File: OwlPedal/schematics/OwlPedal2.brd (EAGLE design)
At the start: 103.1 x 79.5 mm, 86 parts, among them IC1 TS924, J1 NEUTRIK_NMJ6HCD2, J2 NEUTRIK_NMJ6HCD2, J3 NEUTRIK_NMJ6HCD2, J4 NEUTRIK_NMJ6HCD2, J5 NEUTRIK_NMJ6HCD2, J6 NEUTRIK_NMJ6HCD2, J7 POWER_JACK, SW2 5GTH9, U1 TS5A22364

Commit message: adjusted labels
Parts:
- moved R12 0.38 mm to (63.6, 39.4)
- moved R13 0.38 mm to (67.4, 39.4)
- flipped JP2 to the bottom, turned to 180 degrees
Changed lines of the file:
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@@
 </element>
 <element name="R19" library="Rebel" package="0603" value="1k" x="62.5475" y="36.195" smashed="yes" rot="R90">
-<attribute name="NAME" x="62.1095" y="34.584" size="0.762" layer="25" font="vector" rot="R270"/>
+<attribute name="NAME" x="62.2365" y="34.838" size="0.762" layer="25" font="vector" rot="R270"/>
 </element>
 <element name="R5" library="Rebel" package="0603" value="1M" x="69.85" y="58.674" smashed="yes">
@@
 <attribute name="NAME" x="60.66105625" y="37.57635625" size="0.762" layer="25" font="vector" rot="R180" align="bottom-center"/>
 </element>
-<element name="R12" library="Rebel" package="0603" value="1k" x="63.9445" y="39.37" smashed="yes">
-<attribute name="NAME" x="63.913675" y="40.18240625" size="0.762" layer="25" font="vector" align="bottom-center"/>
+<element name="R12" library="Rebel" package="0603" value="1k" x="63.5635" y="39.37" smashed="yes">
+<attribute name="NAME" x="63.532675" y="40.18240625" size="0.762" layer="25" font="vector" align="bottom-center"/>
 </element>
 <element name="R4" library="Rebel" package="0603" value="560R" x="67.3735" y="53.6575" smashed="yes" rot="R270">
@@
 </element>
 <element name="C19" library="resistor" package="C0603" value="4n7 C0G" x="64.516" y="36.195" smashed="yes" rot="R90">
-<attribute name="NAME" x="64.954" y="33.0435" size="0.762" layer="25" font="vector" rot="R90"/>
+<attribute name="NAME" x="64.954" y="32.7895" size="0.762" layer="25" font="vector" rot="R90"/>
 <attribute name="VALUE" x="66.548" y="35.306" size="1.27" layer="27" rot="R90"/>
 </element>
 <element name="C17" library="resistor" package="C0603" value="2n2 C0G" x="58.6105" y="35.433" smashed="yes" rot="R270">
-<attribute name="NAME" x="57.899" y="33.09" size="0.762" layer="25" font="vector"/>
+<attribute name="NAME" x="57.645" y="33.09" size="0.762" layer="25" font="vector"/>
 <attribute name="VALUE" x="56.5785" y="36.322" size="1.27" layer="27" rot="R270"/>
 </element>
@@
 </element>
 <element name="R22" library="Rebel" package="0603" value="1k" x="68.58" y="36.195" smashed="yes" rot="R90">
-<attribute name="NAME" x="68.12374375" y="33.545515625" size="0.762" layer="25" font="vector" rot="R270" align="bottom-center"/>
+<attribute name="NAME" x="68.25074375" y="33.799515625" size="0.762" layer="25" font="vector" rot="R270" align="bottom-center"/>
 </element>
 <element name="R14" library="Rebel" package="0603" value="2k" x="70.5485" y="39.0525" smashed="yes" rot="R90">
 <attribute name="NAME" x="69.6656625" y="39.110025" size="0.762" layer="25" font="vector" rot="R90" align="bottom-center"/>
 </element>
-<element name="R13" library="Rebel" package="0603" value="1k" x="66.9925" y="39.37" smashed="yes" rot="R180">
-<attribute name="NAME" x="67.008525" y="40.20485625" size="0.762" layer="25" font="vector" align="bottom-center"/>
+<element name="R13" library="Rebel" package="0603" value="1k" x="67.3735" y="39.37" smashed="yes" rot="R180">
+<attribute name="NAME" x="67.389525" y="40.20485625" size="0.762" layer="25" font="vector" align="bottom-center"/>
 </element>
 <element name="C15" library="resistor" package="C0603" value="220p C0G" x="71.5645" y="41.656" smashed="yes">
-<attribute name="NAME" x="71.004640625" y="42.235340625" size="0.762" layer="25" font="vector"/>
+<attribute name="NAME" x="70.750640625" y="42.362340625" size="0.762" layer="25" font="vector"/>
 <attribute name="VALUE" x="70.6755" y="39.624" size="1.27" layer="27"/>
 </element>
 <element name="C20" library="resistor" package="C0603" value="4n7 C0G" x="66.6115" y="36.195" smashed="yes" rot="R90">
-<attribute name="NAME" x="66.1735" y="34.584" size="0.762" layer="25" font="vector" rot="R270"/>
+<attribute name="NAME" x="67.0495" y="32.726" size="0.762" layer="25" font="vector" rot="R90"/>
 <attribute name="VALUE" x="68.6435" y="35.306" size="1.27" layer="27" rot="R90"/>
 </element>
@@
 </element>
 <element name="C13" library="resistor" package="C0603" value="1n C0G" x="66.9925" y="41.783" smashed="yes">
-<attribute name="NAME" x="66.3634375" y="42.489965625" size="0.762" layer="25" font="vector"/>
+<attribute name="NAME" x="66.2364375" y="42.489965625" size="0.762" layer="25" font="vector"/>
 <attribute name="VALUE" x="66.1035" y="39.751" size="1.27" layer="27"/>
 </element>
@@
 <attribute name="NAME" x="79.502" y="21.59" size="1.016" layer="25" font="vector" rot="R270" align="bottom-center"/>
 </element>
-<element name="JP2" library="SparkFun" package="1X04" value="" x="53.0225" y="23.8125" smashed="yes">
-<attribute name="VALUE" x="51.7525" y="20.6375" size="1.27" layer="27"/>
+<element name="JP2" library="SparkFun" package="1X04" value="" x="53.0225" y="23.8125" smashed="yes" rot="MR180">
+<attribute name="VALUE" x="51.7525" y="26.9875" size="1.27" layer="28" rot="MR180"/>
 </element>
 <element name="U2" library="Hangar" package="TSR-1-2450" value="" x="33.02" y="48.26" smashed="yes" rot="R180">
@@
 <via x="94.0435" y="49.4665" extent="1-16" drill="0.3048"/>
 <via x="69.469" y="33.655" extent="1-16" drill="0.3048"/>
-<via x="62.23" y="34.163" extent="1-16" drill="0.3048"/>
+<via x="61.849" y="34.29" extent="1-16" drill="0.3048"/>
 <via x="72.8675" y="50.7775" extent="1-16" drill="0.3048"/>
-<via x="61.976" y="40.3225" extent="1-16" drill="0.3048"/>
-<via x="69.1515" y="40.3225" extent="1-16" drill="0.3048"/>
+<via x="61.976" y="40.5765" extent="1-16" drill="0.3048"/>
+<via x="69.1515" y="40.5765" extent="1-16" drill="0.3048"/>
 <via x="96.9645" y="28.0035" extent="1-16" drill="0.3048"/>
 </signal>
@@
 <contactref element="R18" pad="1"/>
 <via x="62.357" y="32.8295" extent="1-16" drill="0.3048"/>
-<wire x1="60.6425" y1="34.583" x2="60.6425" y2="34.544" width="0.3048" layer="1"/>
-<wire x1="62.357" y1="32.8295" x2="60.6425" y2="34.544" width="0.4064" layer="1"/>
+<wire x1="60.6425" y1="34.583" x2="60.6425" y2="34.29" width="0.4064" layer="1"/>
+<wire x1="62.357" y1="32.8295" x2="62.103" y2="32.8295" width="0.4064" layer="1"/>
+<wire x1="62.103" y1="32.8295" x2="60.6425" y2="34.29" width="0.4064" layer="1"/>
 <contactref element="JP9" pad="1"/>
 <wire x1="75.8825" y1="66.9925" x2="78.74" y2="64.135" width="0.4064" layer="1"/>
@@
 <contactref element="IC1" pad="10"/>
 <contactref element="C12" pad="2"/>
-<wire x1="64.7945" y1="39.37" x2="64.7945" y2="40.083" width="0.4064" layer="1"/>
-<wire x1="64.7945" y1="40.083" x2="63.0945" y2="41.783" width="0.4064" layer="1"/>
+<wire x1="64.4135" y1="39.37" x2="64.4135" y2="40.464" width="0.4064" layer="1"/>
+<wire x1="64.4135" y1="40.464" x2="63.0945" y2="41.783" width="0.4064" layer="1"/>
 <wire x1="64.135" y1="45.025" x2="64.135" y2="43.7125" width="0.4064" layer="1"/>
 <wire x1="64.135" y1="43.7125" x2="63.0945" y2="42.672" width="0.4064" layer="1"/>
@@
 <contactref element="R20" pad="2"/>
 <contactref element="C19" pad="1"/>
-<wire x1="63.0945" y1="39.37" x2="62.5865" y2="38.862" width="0.3048" layer="1"/>
-<wire x1="62.5865" y1="38.862" x2="62.5865" y2="37.084" width="0.4064" layer="1"/>
+<wire x1="62.7135" y1="39.37" x2="62.5865" y2="39.243" width="0.3048" layer="1"/>
+<wire x1="62.5865" y1="39.243" x2="62.5865" y2="37.084" width="0.4064" layer="1"/>
 <wire x1="62.5865" y1="37.084" x2="62.5475" y2="37.045" width="0.3048" layer="1"/>
 <wire x1="62.5475" y1="37.045" x2="62.816" y2="37.045" width="0.3048" layer="1"/>
@@
 <contactref element="C13" pad="2"/>
 <wire x1="67.8425" y1="41.783" x2="67.8425" y2="41.451" width="0.4064" layer="1"/>
-<wire x1="67.8425" y1="41.451" x2="66.1425" y2="39.751" width="0.4064" layer="1"/>
-<wire x1="66.1425" y1="39.751" x2="66.1425" y2="39.37" width="0.4064" layer="1"/>
+<wire x1="67.8425" y1="41.451" x2="66.5235" y2="40.132" width="0.4064" layer="1"/>
+<wire x1="66.5235" y1="40.132" x2="66.5235" y2="39.37" width="0.4064" layer="1"/>
 <wire x1="66.675" y1="45.025" x2="66.675" y2="43.7125" width="0.4064" layer="1"/>
 <wire x1="67.8425" y1="42.545" x2="66.675" y2="43.7125" width="0.4064" layer="1"/>
@@
 <wire x1="66.6115" y1="35.345" x2="66.675" y2="35.2815" width="0.4064" layer="1"/>
 <wire x1="66.675" y1="35.2815" x2="66.675" y2="32.092" width="0.4064" layer="1"/>
-<wire x1="67.8425" y1="39.37" x2="67.8425" y2="39.1795" width="0.4064" layer="1"/>
-<wire x1="68.58" y1="38.442" x2="67.8425" y2="39.1795" width="0.4064" layer="1"/>
+<wire x1="68.2235" y1="39.37" x2="68.2235" y2="38.7985" width="0.4064" layer="1"/>
+<wire x1="68.58" y1="38.442" x2="68.2235" y2="38.7985" width="0.4064" layer="1"/>
 <wire x1="68.58" y1="38.442" x2="68.58" y2="37.045" width="0.4064" layer="1"/>
 <wire x1="68.58" y1="37.045" x2="68.3115" y2="37.045" width="0.4064" layer="1"/>

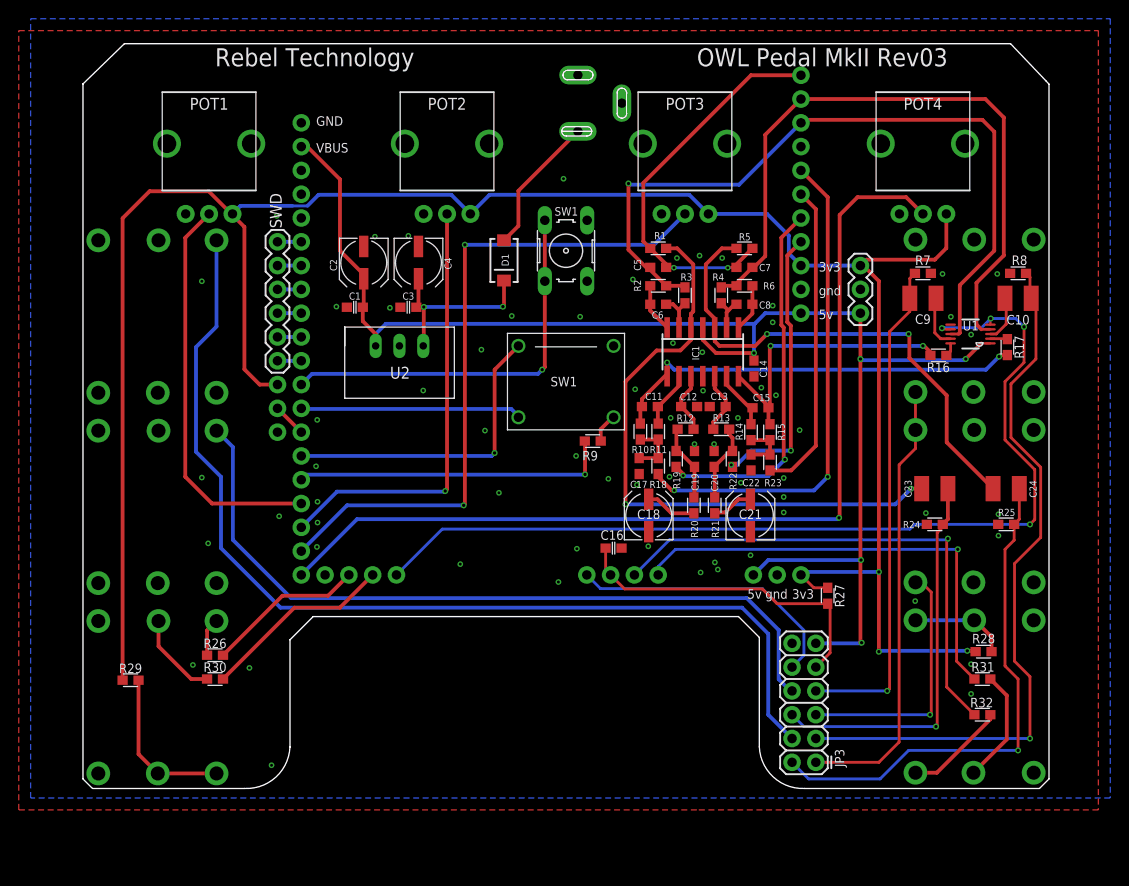
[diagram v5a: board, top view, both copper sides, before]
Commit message: Removed analog switch. Rev04
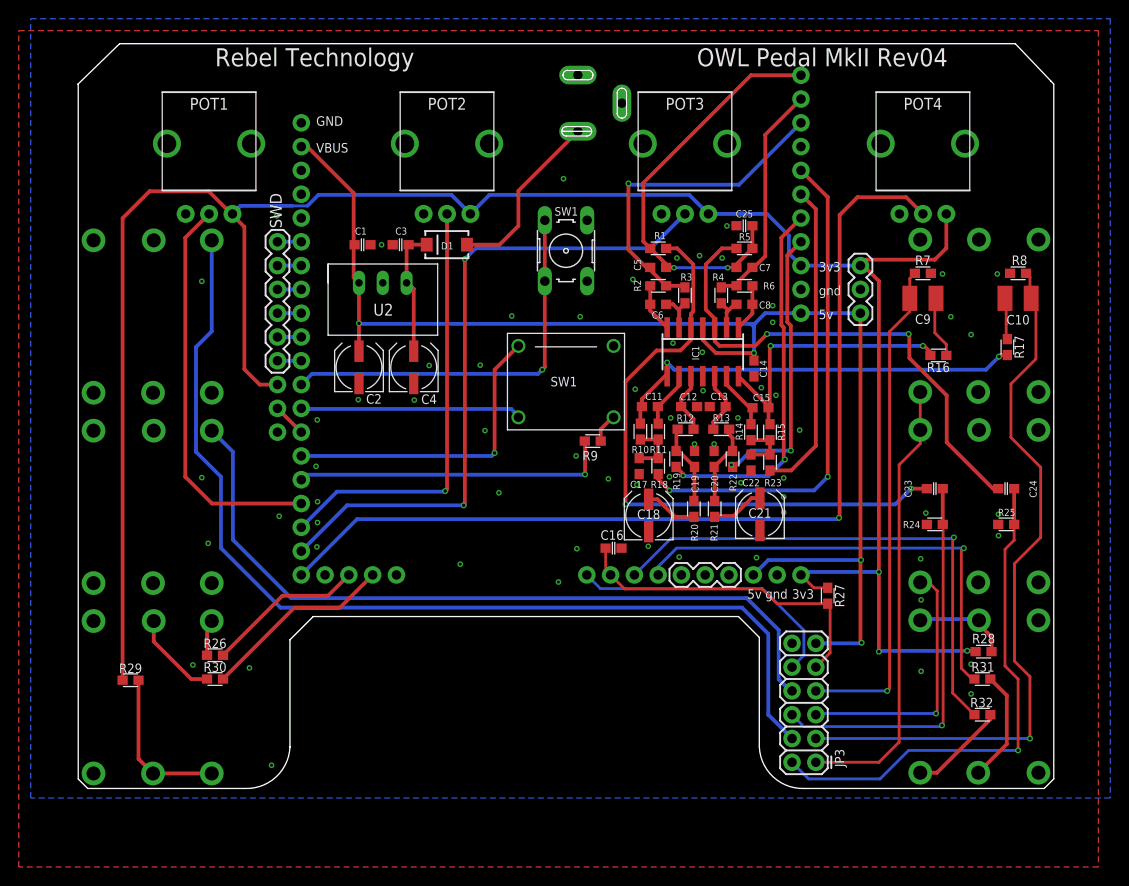
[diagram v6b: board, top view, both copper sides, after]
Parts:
- removed U1: TS5A22364, Rebel:DGS0010A_L
- added C25: 100n, Rebel:C0603
- added JP12: (no value), SparkFun:1X03
- C23, C24: value 10n Film -> 10n C0G; device Rebel:C1210 -> Rebel:C0603
- C3: value 100n 16v -> 100n
- R24, R25: value 1M -> 10M
- moved C2 11.2 mm to (28.7, 46.0), turned to 90 degrees
- moved C4 11.2 mm to (34.5, 46.0), turned to 90 degrees
- moved U2 6.96 mm to (31.2, 55.0)
- moved C1 6.72 mm to (29.1, 59.1), turned to 0 degrees
- moved C3 6.72 mm to (33.1, 59.1)
- moved D1 6.33 mm to (38.1, 59.1), turned to 180 degrees
- moved C21 1.02 mm to (71.5, 30.3)
- moved J1 0.51 mm to (95.1, 10.8)
- moved J3 0.51 mm to (95.1, 31.1)
- moved J5 0.51 mm to (95.1, 51.4)
- moved J2 0.51 mm to (6.48, 10.8)
- moved J4 0.51 mm to (6.48, 31.1)
- moved J6 0.51 mm to (6.48, 51.4)
- moved R20 0.38 mm to (64.5, 30.9)
- moved R21 0.38 mm to (66.7, 30.9)
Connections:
- removed net N$11: R17.1, U1.2
- removed net N$27: C10.1, U1.3
- removed net N$37: R16.1, U1.10
- new net N$35: C10.1, R17.1
- net +5V: no longer U1.1
- net A25: no longer U1.5, U1.7
- net AIN_A: no longer U1.4
- net AIN_B: no longer U1.8
- net CS_VREF: now also C25.1
- net GND: now also C25.2; no longer U1.6
- net N$30: now also R16.1; no longer U1.9
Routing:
- net A25: track 104.5 -> 0.00 mm, vias 4 -> 0
- net AIN_A: track 72.1 -> 24.6 mm
- net AIN_B: track 81.4 -> 36.1 mm
- net +5V: track 157.5 -> 143.1 mm, vias 5 -> 4
- net N$51: track 19.4 -> 13.8 mm, vias 2 -> 0
- net N$27: track 4.93 -> 0.00 mm
- net N$35: track 0.00 -> 4.46 mm
- net +9V: track 14.9 -> 19.0 mm
- net CS_VREF: track 41.9 -> 44.3 mm
- net N$11: track 1.83 -> 0.00 mm
- net N$37: track 1.47 -> 0.00 mm
- net N$31: track 4.43 -> 5.66 mm
- net N$30: track 5.68 -> 6.66 mm
- net A20_ADC3: track 72.1 -> 71.2 mm
- net IN_R: track 27.4 -> 28.3 mm
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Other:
- board size 103.1 x 79.5 mm -> 104.2 x 79.5 mm
- board text added: "OWL Pedal MkII Rev04"
- board text added: "STEREO"
- board text removed: "OWL Pedal MkII Rev03"
